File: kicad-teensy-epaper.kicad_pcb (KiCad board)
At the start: 2 copper layers, 0 parts

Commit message: create small board to test footprint
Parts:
- added J1: HEADER-FEMALE-34POS-FFC-SMT-1x34-P0.5MM, Wickerlib:CONN-HEADER-FH34SRJ-34S-0.5SH, F.Cu at (147.0, 97.8)
- added W6: A5, Wickerlib:CONN-HEADER-STRAIGHT-P2.54MM-1x01, F.Cu at (147.1, 84.5)
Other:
- board outline added: 9.3 x 28.3 mm
- net class Default: clearance 0.2 -> 0.127; trace_width 0.25 -> 0.127; via_dia 0.6 -> 0.3556; via_drill 0.4 -> 0.254
- rule pad_to_mask_clearance: 0.2 -> 0.0762
- rule trace_clearance: 0.2 -> 0.127
- rule trace_min: 0.2 -> 0.127
- rule via_min_drill: 0.3 -> 0.254
- rule via_min_size: 0.4 -> 0.3556
- board text added: "KiCad"
- board text added: "Thanks, Wickerlib!"

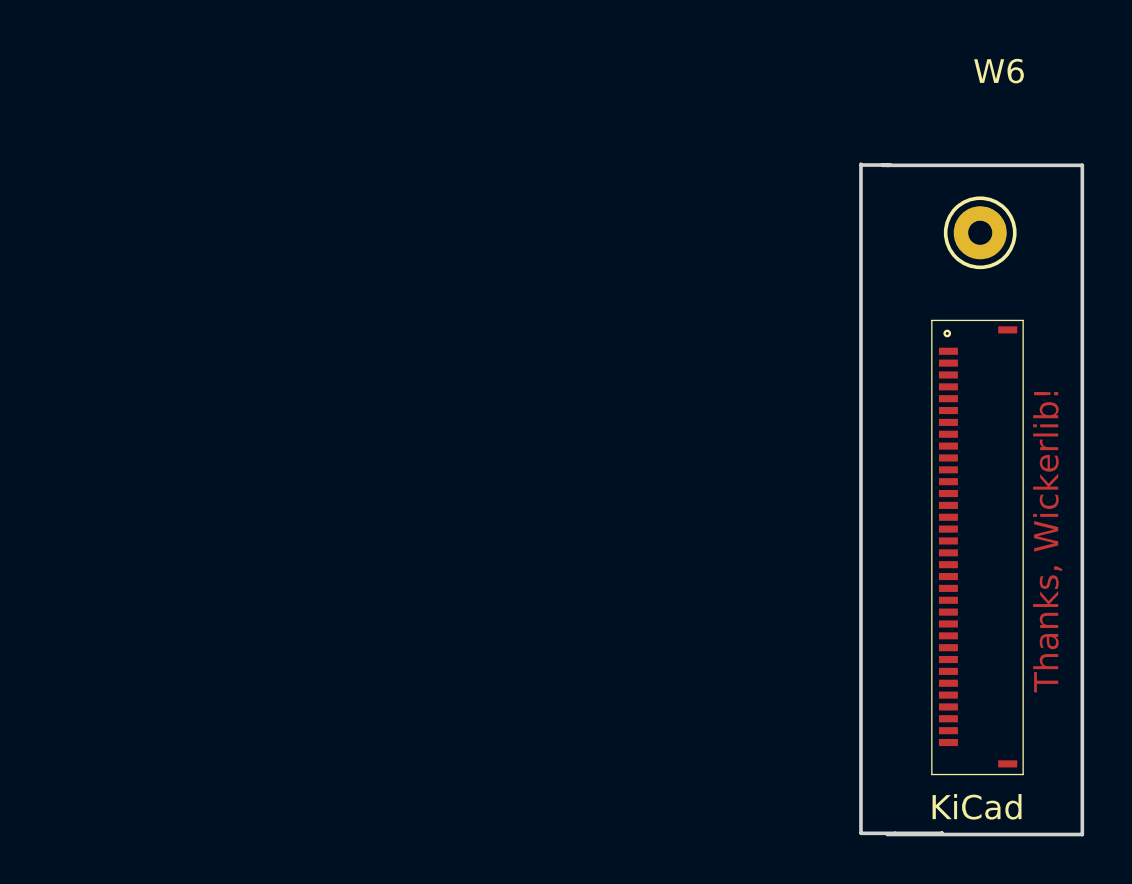
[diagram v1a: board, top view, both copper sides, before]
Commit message: start the schematic and layout over
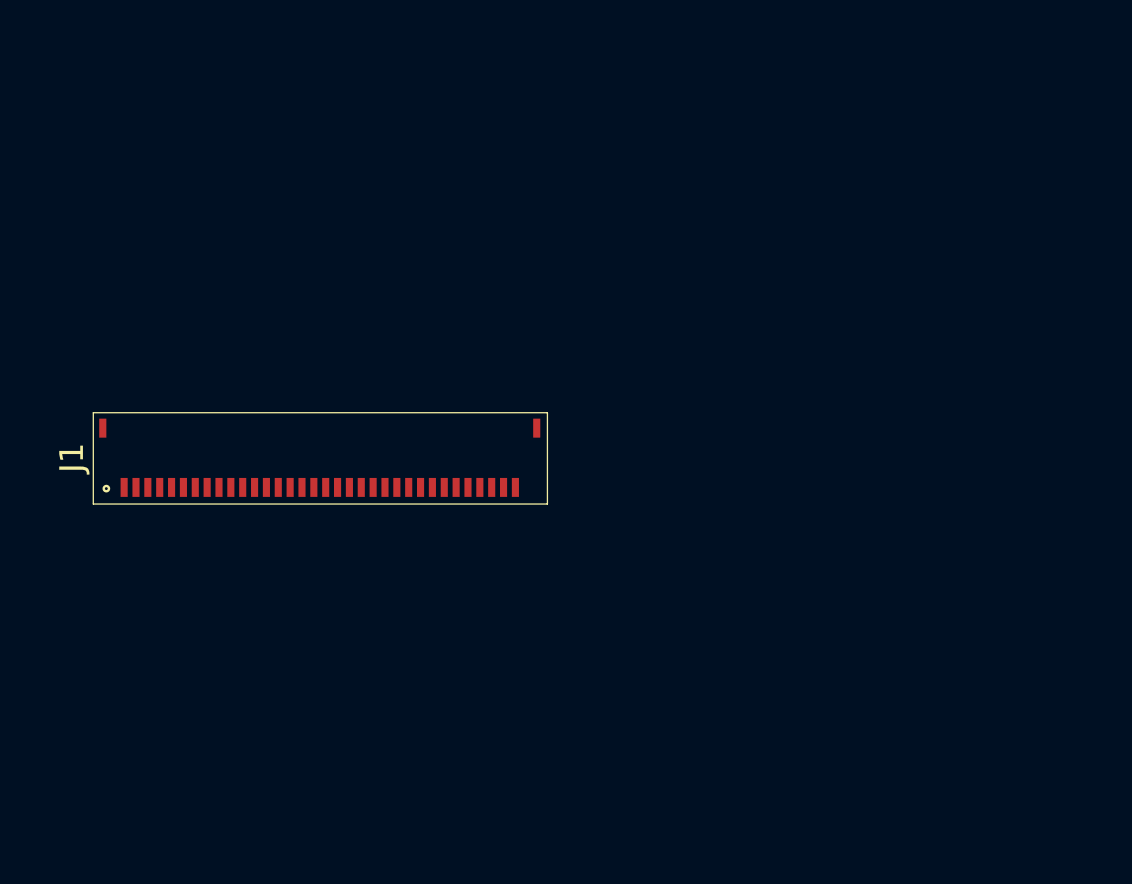
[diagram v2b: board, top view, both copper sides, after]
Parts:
- removed W6: A5, Wickerlib:CONN-HEADER-STRAIGHT-P2.54MM-1x01
- moved J1 28.0 mm to (119.3, 94.1), turned to 0 degrees
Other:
- board outline removed
- board text removed: "KiCad"
- board text removed: "Thanks, Wickerlib!"

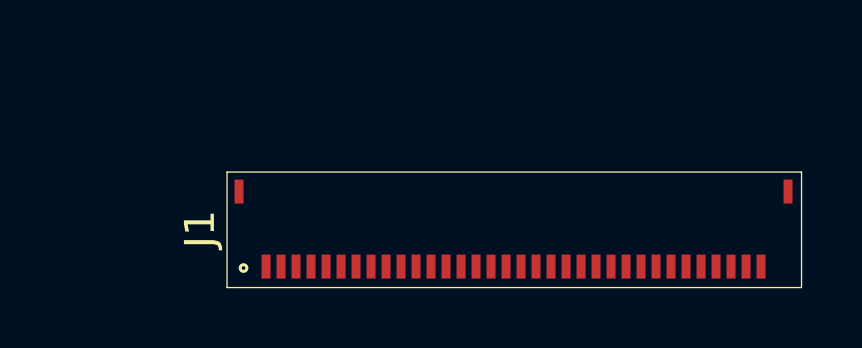
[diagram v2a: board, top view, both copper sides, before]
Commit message: finish redrawing the EAGLE schematic in KiCad
TODO: make sure the correct parts are used for passives and mosfet
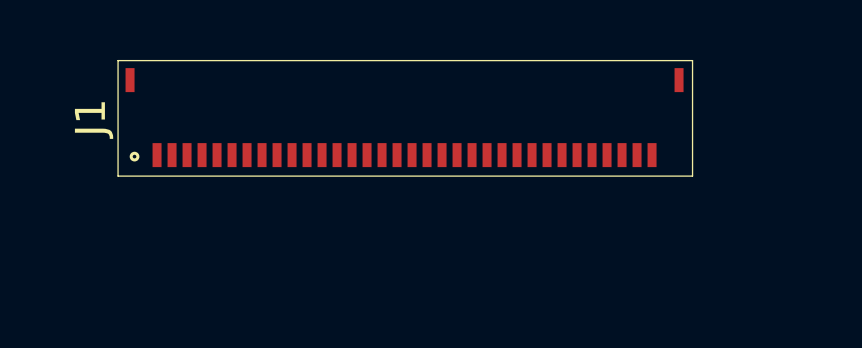
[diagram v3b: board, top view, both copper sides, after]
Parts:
- moved J1 5.20 mm to (115.6, 90.4)
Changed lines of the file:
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@@
     (links 2)
     (no_connects 2)
-    (area 0 0 0 0)
+    (area 99.911715 74.854999 178.510001 123.265001)
     (thickness 1.6)
     (drawings 17)
@@
     (pad_to_paste_clearance -0.0762)
     (aux_axis_origin 196.5452 123.5456)
-    (visible_elements FFFFFFFF)
+    (visible_elements FFFFEFFF)
     (pcbplotparams
       (layerselection 0x310fc_80000001)
@@
   )
   (module Wickerlib:CONN-HEADER-FH34SRJ-34S-0.5SH (layer F.Cu)
-    (at 119.253 94.107)
+    (at 115.62 90.392)
     (fp_text reference J1 (at -0.225 -0.325 180) (layer F.Fab)
       (effects (font (size 1 1) (thickness 0.15)))

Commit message: first attempt at layout, 1 air wire remains
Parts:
- added C1: CAP-CER-1UF, Capacitors_SMD:C_0805_HandSoldering, F.Cu at (98.9, 35.0)
- added C10: CAP-CER-1UF, Capacitors_SMD:C_0805_HandSoldering, F.Cu at (98.9, 53.4)
- added C2: CAP-CER-1UF, Capacitors_SMD:C_0805_HandSoldering, F.Cu at (110.3, 35.0)
- added C3: CAP-CER-1UF, Capacitors_SMD:C_0805_HandSoldering, F.Cu at (121.7, 35.0)
- added C4: CAP-CER-1UF, Capacitors_SMD:C_0805_HandSoldering, F.Cu at (98.9, 41.1)
- added C5: CAP-CER-1UF, Capacitors_SMD:C_0805_HandSoldering, F.Cu at (110.3, 41.1)
- added C6: CAP-CER-1UF, Capacitors_SMD:C_0805_HandSoldering, F.Cu at (121.7, 41.1)
- added C7: CAP-CER-1UF, Capacitors_SMD:C_0805_HandSoldering, F.Cu at (98.9, 47.3)
- added C8: CAP-CER-1UF, Capacitors_SMD:C_0805_HandSoldering, F.Cu at (110.3, 47.3)
- added C9: CAP-CER-1UF, Capacitors_SMD:C_0805_HandSoldering, F.Cu at (121.7, 47.3)
- added D1: DIODE, Diodes_SMD:SOD-123, F.Cu at (160.8, 30.0)
- added D2: DIODE, Diodes_SMD:SOD-123, F.Cu at (160.8, 36.2)
- added D3: DIODE, Diodes_SMD:SOD-123, F.Cu at (160.5, 42.0)
- added J2: HEADER-FEMALE-34POS-FFC-SMT-1x34-P0.5MM, Wickerlib:CONN-HEADER-FH34SRJ-34S-0.5SH, F.Cu at (112.6, 28.0)
- added L1: INDUCTOR, Inductors:Inductor_1212, F.Cu at (118.4, 54.1)
- added Q1: Q_NMOS_GDS, TO_SOT_Packages_SMD:SOT-23_Handsoldering, F.Cu at (109.6, 55.1)
- added R1: 2.2R 1%, Resistors_SMD:R_0805_HandSoldering, F.Cu at (125.6, 53.4)
- J1: value HEADER-FEMALE-34POS-FFC-SMT-1x34-P0.5MM -> TEENSY3.2-72MHz; footprint Wickerlib:CONN-HEADER-FH34SRJ-34S-0.5SH -> Wickerlib:TEENSY-3.2-SILK
- moved J1 59.8 mm to (143.6, 37.5)
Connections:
- J1 pad 11: Net-(J1-Pad11) -> DOUT
- J1 pad 13: Net-(J1-Pad13) -> SCK
- J1 pad 14: Net-(J1-Pad14) -> ^RES
- J1 pad 15: Net-(J1-Pad15) -> BUSY
- J1 pad 16: Net-(J1-Pad16) -> ^D/C
- J1 pad 17: Net-(J1-Pad17) -> ^CS
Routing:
- net BS1: track 0.00 -> 143.5 mm, vias 0 -> 9
- net Net-(C2-Pad2): track 0.00 -> 87.5 mm, vias 0 -> 4
- net PRVGL: track 0.00 -> 72.5 mm, vias 0 -> 6
- net Net-(C2-Pad1): track 0.00 -> 69.6 mm, vias 0 -> 2
- net VDDIO: track 0.00 -> 68.4 mm, vias 0 -> 3
- net ^RES: track 0.00 -> 56.1 mm, vias 0 -> 3
- net SCK: track 0.00 -> 55.1 mm, vias 0 -> 2
- net VGH: track 0.00 -> 53.9 mm, vias 0 -> 4
- net BUSY: track 0.00 -> 52.2 mm, vias 0 -> 5
- net ^D/C: track 0.00 -> 51.0 mm, vias 0 -> 3
- net ^CS: track 0.00 -> 48.7 mm, vias 0 -> 3
- net RESE: track 0.00 -> 43.8 mm, vias 0 -> 4
- net VSL: track 0.00 -> 39.6 mm, vias 0 -> 4
- net DOUT: track 0.00 -> 38.7 mm, vias 0 -> 2
- net VSH: track 0.00 -> 31.3 mm, vias 0 -> 2
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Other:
- board outline added: 69 x 42.4 mm
- net class Default: via_dia 0.3556 -> 0.6858; via_drill 0.254 -> 0.3302
- rule via_min_drill: 0.254 -> 0.3302
- rule via_min_size: 0.3556 -> 0.6858

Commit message: order new version
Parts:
- added R2: RES-0.0-JUMPER-1/8W-0603, RLC-0603-SMD, F.Cu at (111.8, 74.0)
- C1, C10, C2, C3, C4, C5, C6, C7, C8, C9, D1, D2, D3, L1, Q1, R1: moved to B.Cu
- moved D1 77.2 mm to (102.1, 80.1), turned to 270 degrees
- moved D3 65.9 mm to (106.7, 80.1), turned to 90 degrees
- moved D2 58.8 mm to (104.6, 53.5), turned to 180 degrees
- moved C4 49.7 mm to (135.7, 74.4), turned to 180 degrees
- moved C2 47.3 mm to (97.5, 80.5), turned to 90 degrees
- moved C10 40.2 mm to (135.5, 70.1), turned to 180 degrees
- moved C7 39.5 mm to (135.5, 61.9), turned to 180 degrees
- moved J2 35.1 mm to (112.4, 63.1), turned to 90 degrees
- moved J1 34.9 mm to (155.2, 70.5), turned to 180 degrees
- moved C9 33.9 mm to (135.7, 78.1), turned to 180 degrees
- moved C8 31.3 mm to (135.4, 65.9), turned to 180 degrees
- moved C6 29.8 mm to (105.0, 65.8)
- moved C1 29.0 mm to (105.0, 63.3)
- moved C5 28.4 mm to (135.6, 54.0), turned to 180 degrees
- moved C3 26.9 mm to (135.6, 58.0), turned to 180 degrees
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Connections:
- net BS1 renamed GND
- net NC1 renamed Net-(J2-Pad1)
- net NC3 renamed Net-(J2-Pad3)
- net NC4 renamed Net-(J2-Pad4)
- net NC5 renamed Net-(J2-Pad5)
- net NC7 renamed Net-(J2-Pad30)
- J2 pad 10: VGH -> VSH
- J2 pad 11: TSCL -> VPP
- J2 pad 12: TSDA -> VDD
- J2 pad 14: BUSY -> VDDIO
- J2 pad 15: ^RES -> VDDIO
- J2 pad 16: ^D/C -> DOUT
- J2 pad 17: ^CS -> SCK
- J2 pad 18: SCK -> ^CS
- J2 pad 19: DOUT -> ^D/C
- J2 pad 2: NC2 -> Net-(J2-Pad2)
- J2 pad 20: VDDIO -> ^RES
- J2 pad 21: VDDIO -> BUSY
- J2 pad 23: VDD -> TSDA
- J2 pad 24: VPP -> TSCL
- J2 pad 25: VSH -> VGH
- J2 pad 26: VGH2 -> VGL
- J2 pad 27: VSL -> RESE
- J2 pad 28: PRVGL -> GDR
- J2 pad 29: VCOM -> Net-(J2-Pad29)
- J2 pad 31: NC8 -> Net-(J2-Pad31)
- J2 pad 32: NC8 -> Net-(J2-Pad32)
- J2 pad 33: NC8 -> Net-(J2-Pad33)
- J2 pad 34: NC8 -> Net-(J2-Pad34)
- J2 pad 6: NC6 -> VCOM
- J2 pad 7: GDR -> PRVGL
- J2 pad 8: RESE -> VSL
- J2 pad 9: VGL -> VGH2
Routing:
- net GND: track 143.5 -> 13.3 mm, vias 9 -> 4
- net Net-(C2-Pad1): track 69.6 -> 9.24 mm, vias 2 -> 0
- net Net-(C2-Pad2): track 87.5 -> 40.5 mm, vias 4 -> 0
- net PRVGL: track 72.5 -> 38.9 mm, vias 6 -> 2
- net Net-(J2-Pad2): track 0.00 -> 26.8 mm, vias 0 -> 2
- net NC2: track 21.8 -> 0.00 mm, vias 2 -> 0
- net DOUT: track 38.7 -> 57.5 mm, vias 2 -> 1
- net VGH: track 53.9 -> 35.1 mm, vias 4 -> 2
- net VSL: track 39.6 -> 21.7 mm, vias 4 -> 1
- net ^RES: track 56.1 -> 43.7 mm
- net GDR: track 28.5 -> 18.0 mm, vias 0 -> 1
- net VDD: track 17.5 -> 7.26 mm, vias 4 -> 1
- net VGL: track 13.3 -> 22.8 mm, vias 0 -> 1
- net ^D/C: track 51.0 -> 59.8 mm
- net ^CS: track 48.7 -> 40.1 mm, vias 3 -> 1
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- added copper zone on B.Cu, net GND
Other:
- board size 69 x 42.4 mm -> 80.2 x 42.1 mm
- net class Default: clearance 0.127 -> 0.1524; trace_width 0.127 -> 0.1524
- rule trace_clearance: 0.127 -> 0.1524
- rule trace_min: 0.127 -> 0.1524
- board text added: "JUMPER"
- board text added: "pdp7/kicad-teensy-epaper 2017-03-29"

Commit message: make ground pads bigger on FPC 34-pos connector
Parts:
- removed R2: RES-0.0-JUMPER-1/8W-0603, RLC-0603-SMD
- J2: footprint Wickerlib:CONN-HEADER-FH34SRJ-34S-0.5SH -> hirose-34pos-bigger-gnd-pads:CONN-HEADER-FH34SRJ-34S-0.5SH-BIG-GND
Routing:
- net Net-(J2-Pad2): track 26.8 -> 0.00 mm, vias 2 -> 0
- net ^D/C: track 59.8 -> 60.7 mm

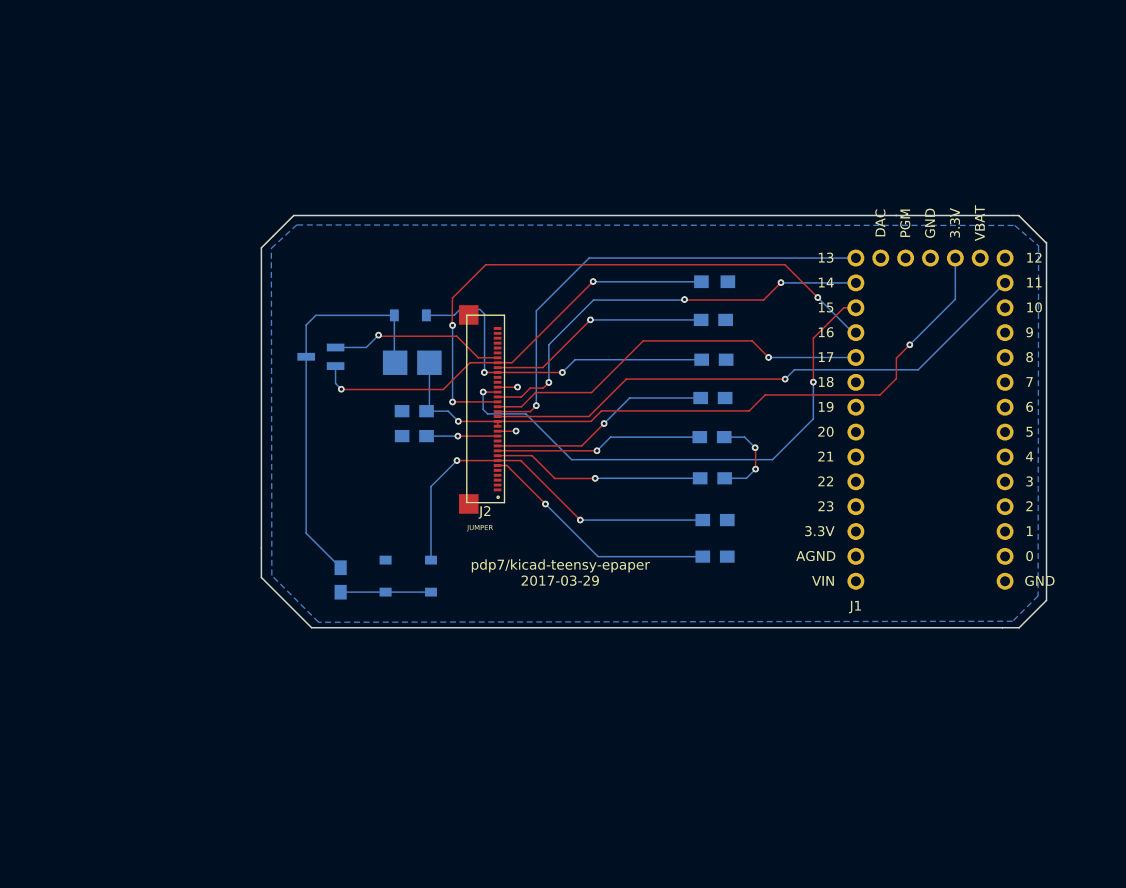
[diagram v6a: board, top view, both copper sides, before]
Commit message: added slot and rerouted traces
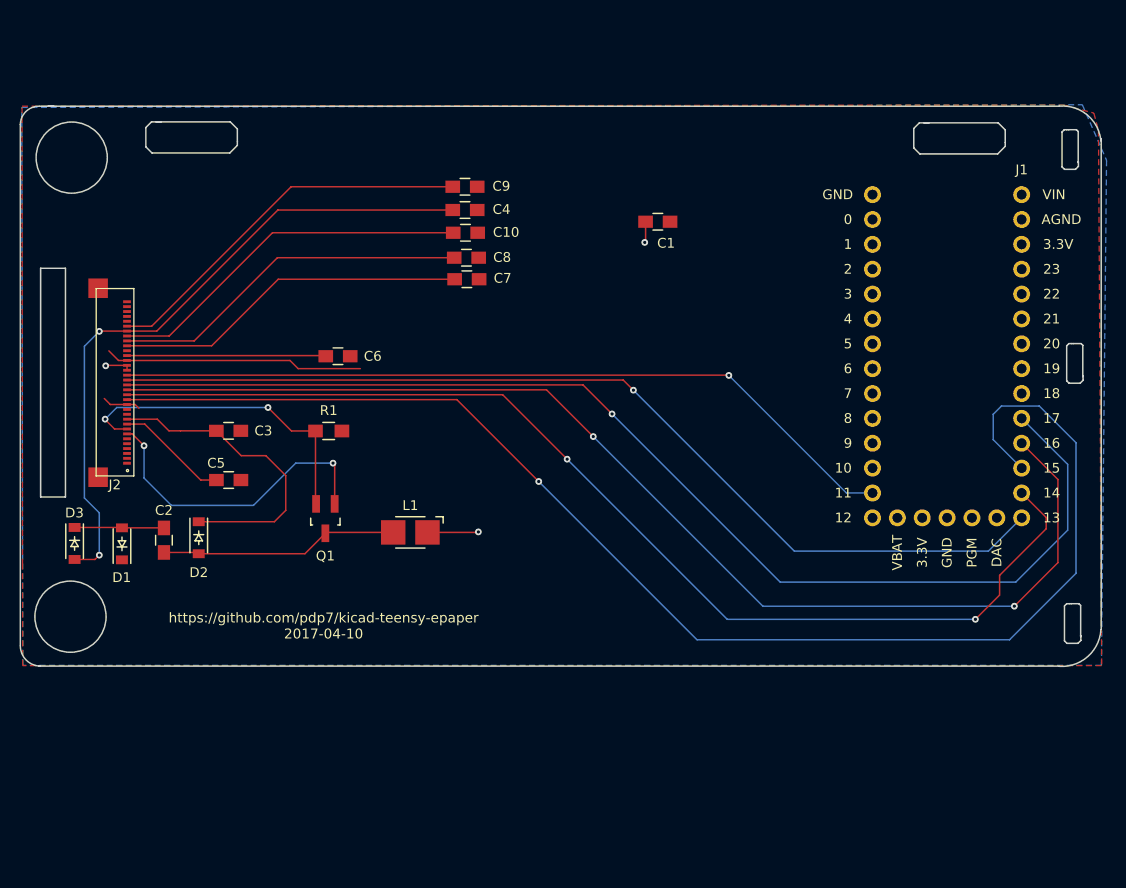
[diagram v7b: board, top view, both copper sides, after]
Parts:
- C1, C10, C3, C4, C5, C6, C7, C8, C9, D1, D2, D3, L1, Q1, R1: moved to F.Cu
- C2: value CAP-CER-1UF -> CAP-CER-2.2UF; moved to F.Cu
- moved C5 52.2 mm to (86.1, 70.3)
- moved C3 50.1 mm to (86.1, 65.3)
- moved C9 45.6 mm to (110.2, 40.4)
- moved R1 42.3 mm to (96.3, 65.3)
- moved C4 40.7 mm to (110.2, 42.7)
- moved J2 38.0 mm to (74.5, 60.4)
- moved D3 36.6 mm to (70.3, 76.8), turned to 270 degrees
- moved C10 35.6 mm to (110.3, 45.1)
- moved C1 31.5 mm to (129.9, 43.9), turned to 180 degrees
- moved D2 31.4 mm to (83.0, 76.2), turned to 270 degrees
- moved C8 31.1 mm to (110.4, 47.6)
- moved C7 27.9 mm to (110.4, 49.8)
- moved D1 27.1 mm to (75.2, 76.8), turned to 90 degrees
- moved J1 20.3 mm to (162.0, 51.3), turned to 0 degrees
- moved C2 18.5 mm to (79.4, 76.5), turned to 270 degrees
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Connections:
- J2 pad 10: VSH -> VGH
- J2 pad 11: VPP -> Net-(J2-Pad11)
- J2 pad 12: VDD -> Net-(J2-Pad12)
- J2 pad 14: VDDIO -> BUSY
- J2 pad 15: VDDIO -> ^RES
- J2 pad 16: DOUT -> ^D/C
- J2 pad 17: SCK -> ^CS
- J2 pad 18: ^CS -> SCK
- J2 pad 19: ^D/C -> DOUT
- J2 pad 20: ^RES -> VDDIO
- J2 pad 21: BUSY -> VDDIO
- J2 pad 23: TSDA -> VDD
- J2 pad 24: TSCL -> VPP
- J2 pad 25: VGH -> VSH
- J2 pad 26: VGL -> VGH2
- J2 pad 27: RESE -> VSL
- J2 pad 28: GDR -> PRVGL
- J2 pad 29: Net-(J2-Pad29) -> VCOM
- J2 pad 6: VCOM -> Net-(J2-Pad6)
- J2 pad 7: PRVGL -> GDR
- J2 pad 8: VSL -> RESE
- J2 pad 9: VGH2 -> VGL
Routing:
- net BUSY: track 54.7 -> 140.6 mm, vias 2 -> 1
- net ^CS: track 40.1 -> 120.0 mm
- net ^RES: track 43.7 -> 113.1 mm, vias 3 -> 2
- net VDDIO: track 70.6 -> 10.1 mm, vias 2 -> 3
- net ^D/C: track 60.7 -> 119.8 mm, vias 3 -> 2
- net SCK: track 48.8 -> 100.0 mm
- net PRVGL: track 38.9 -> 68.1 mm
- net DOUT: track 57.5 -> 81.1 mm
- net GND: track 13.3 -> 30.4 mm, vias 4 -> 0
- net Net-(C2-Pad2): track 40.5 -> 24.4 mm
- net VSL: track 21.7 -> 37.7 mm, vias 1 -> 0
- net VGH2: track 21.2 -> 36.9 mm, vias 1 -> 0
- net VCOM: track 24.8 -> 39.2 mm, vias 1 -> 0
- net GDR: track 18.0 -> 32.0 mm, vias 1 -> 2
- net VSH: track 22.8 -> 36.3 mm, vias 1 -> 0
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- added copper zone on F.Cu, net GND
- added copper zone on B.Cu, net VDDIO
- removed copper zone on B.Cu, net GND
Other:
- board size 80.2 x 42.1 mm -> 110.4 x 57.2 mm
- board text added: "Drew Fustini drew@oshpark.com"
- board text added: "github.com/pdp7/kicad-teensy-epaper"
- board text added: "https://github.com/pdp7/kicad-teensy-epaper 2017-04-10"
- board text removed: "JUMPER"
- board text removed: "pdp7/kicad-teensy-epaper 2017-03-29"
